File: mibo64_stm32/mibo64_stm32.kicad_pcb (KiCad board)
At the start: 2 copper layers, 73.7 x 20.3 mm, 36 parts, among them J1 Conn_01x02, J2 Conn_01x29, J3 Conn_01x29, J4 USB_B_Micro, J5 Conn_01x04, SW1 Reset, U1 STM32F405RGTx, U2 AMS1117-3.3, Y1 8MHz, Y2 32.768kHz

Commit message: almost fully routed
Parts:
- C12, C13: value 1uF -> 2.2uF
- moved C12 19.5 mm to (133.4, 119.3)
- moved R4 10.1 mm to (137.4, 106.6), turned to 180 degrees
- moved C13 8.16 mm to (151.4, 115.8)
- moved C11 7.67 mm to (163.6, 117.3), turned to 180 degrees
- moved C8 6.37 mm to (167.4, 117.3)
- moved C4 6.34 mm to (147.4, 106.9), turned to 180 degrees
- moved R2 5.76 mm to (155.7, 111.3), turned to 90 degrees
- moved C5 5.39 mm to (152.1, 113.0), turned to 90 degrees
- moved SW1 5.34 mm to (158.8, 112.8), turned to 270 degrees
- moved C3 4.44 mm to (155.7, 114.5), turned to 270 degrees
- moved C7 3.84 mm to (133.2, 115.4), turned to 180 degrees
- moved U2 3.07 mm to (165.4, 111.8)
- moved J1 2.54 mm to (111.8, 111.8), turned to 180 degrees
- moved C10 2.49 mm to (121.9, 108.7), turned to 270 degrees
- moved Y2 2.01 mm to (118.1, 108.0)
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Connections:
- J2 pad 10: /PA5 -> /PB0
- J2 pad 11: /PA6 -> /PB1
- J2 pad 12: /PA7 -> /PB11
- J2 pad 13: /PA8 -> /PB10
- J2 pad 14: /PA9 -> /PB2
- J2 pad 15: /PA10 -> /PB12
- J2 pad 16: /PA11 -> /PB13
- J2 pad 17: /PA12 -> /PB14
- J2 pad 18: /PA15 -> /PB15
- J2 pad 19: /PC0 -> /PC6
- J2 pad 20: /PC1 -> /PC7
- J2 pad 21: /PC2 -> /PC8
- J2 pad 22: /PC3 -> /PC9
- J2 pad 23: /PC4 -> /PA8
- J2 pad 24: /PC5 -> /PA9
- J2 pad 25: /PC6 -> /PA10
- J2 pad 26: /PC7 -> /PA11
- J2 pad 27: /OSC32_IN -> /PA12
- J2 pad 3: /RESET -> /PA3
- J2 pad 4: /VBAT -> /PA4
- J2 pad 5: /PA0 -> /PA5
- J2 pad 6: /PA1 -> /PA6
- J2 pad 7: /PA2 -> /PA7
- J2 pad 8: /PA3 -> /PC4
- J2 pad 9: /PA4 -> /PC5
- J3 pad 10: /PB5 -> /PC3
- J3 pad 11: /PB6 -> /PC2
- J3 pad 12: /PB7 -> /PC1
- J3 pad 13: /PB8 -> /PC0
- J3 pad 14: /PB9 -> /VBAT
- J3 pad 15: /PB10 -> /PB8
- J3 pad 16: /PB11 -> /PB9
- J3 pad 17: /PB12 -> /PB7
- J3 pad 18: /PB13 -> /PB6
- J3 pad 19: /PB14 -> /PB5
- J3 pad 20: /PB15 -> /PB4
- J3 pad 21: /PC8 -> /PB3
- J3 pad 22: /PC9 -> /PD2
- J3 pad 23: /PC10 -> /PC12
- J3 pad 25: /PC12 -> /PC10
- J3 pad 26: /LED1 -> /PA15
- J3 pad 27: /OSC32_OUT -> /LED1
- J3 pad 4: /PD2 -> /OSC32_IN
- J3 pad 5: /PB0 -> /OSC32_OUT
- J3 pad 6: /PB1 -> /RESET
- J3 pad 7: /PB2 -> /PA2
- J3 pad 8: /PB3 -> /PA1
- J3 pad 9: /PB4 -> /PA0
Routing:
- net GND: track 0.00 -> 40.4 mm, vias 0 -> 13
- net /LED1: track 0.00 -> 37.7 mm, vias 0 -> 2
- net +3V3: track 0.00 -> 33.5 mm, vias 0 -> 6
- net /RESET: track 0.00 -> 33.0 mm
- net /PA15: track 0.00 -> 32.8 mm, vias 0 -> 1
- net /PA12: track 0.00 -> 30.6 mm
- net /PA3: track 0.00 -> 29.0 mm
- net /PA11: track 0.00 -> 27.9 mm
- net /PA4: track 0.00 -> 25.9 mm
- net /PA5: track 0.00 -> 23.5 mm
- net /PA10: track 0.00 -> 22.9 mm
- net /PC10: track 0.00 -> 22.2 mm
- net /PA6: track 0.00 -> 21.2 mm
- net /PA9: track 0.00 -> 20.5 mm
- net /PC11: track 0.00 -> 19.9 mm
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- added copper zone on B.Cu, net GND
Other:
- net class Default: clearance 0.2 -> 0.152; trace_width 0.25 -> 0.152; via_dia 0.8 -> 0.6; via_drill 0.4 -> 0.3
- net class power added: clearance 0.152, trace_width 0.4, via_dia 0.8, via_drill 0.5
- rule trace_clearance: 0.2 -> 0.152
- rule trace_min: 0.2 -> 0.152
- board text added: "GND"

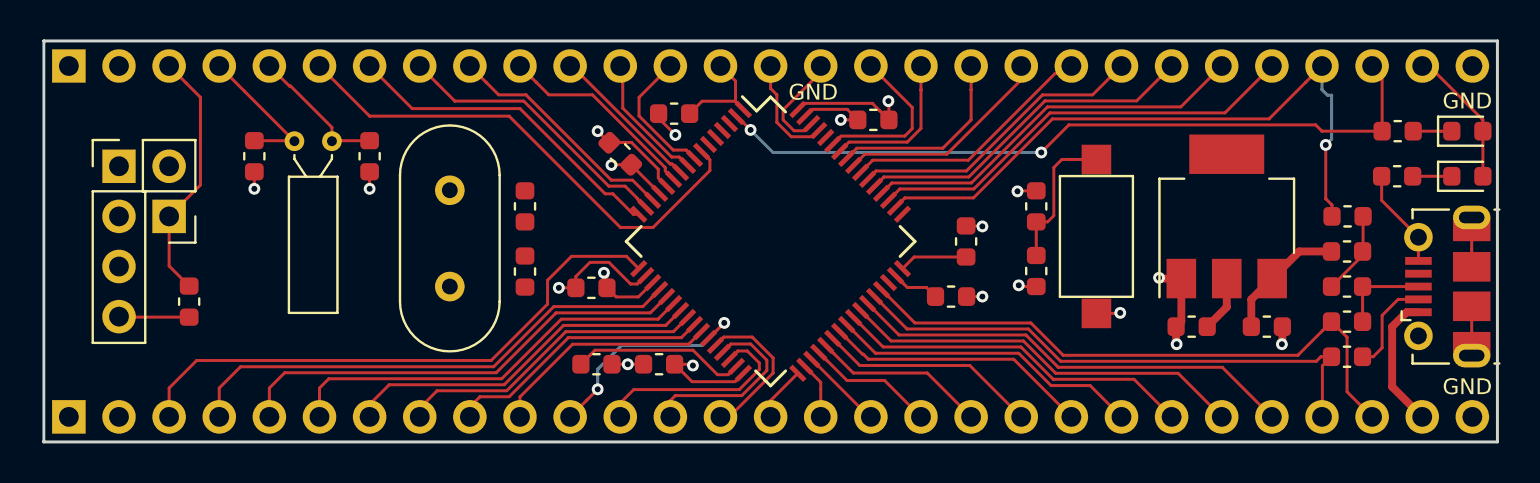
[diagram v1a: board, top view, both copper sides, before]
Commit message: fully routed, labelling still missing
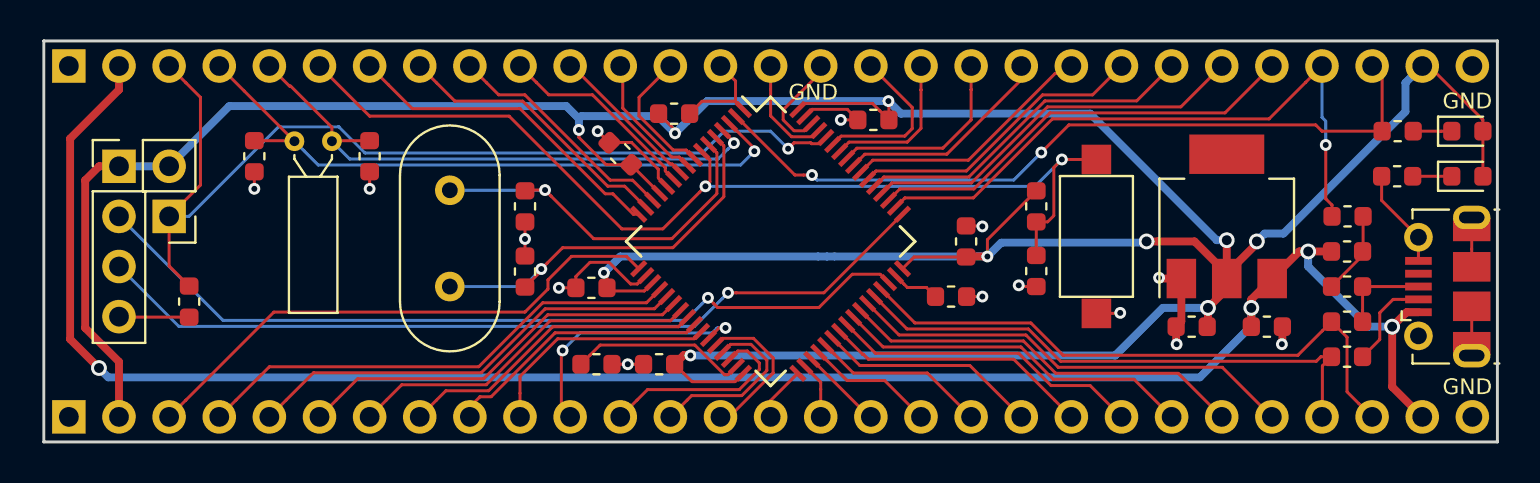
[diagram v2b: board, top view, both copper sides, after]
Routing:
- net +3V3: track 33.5 -> 194.8 mm, vias 6 -> 10
- net /5V: track 13.3 -> 97.1 mm, vias 0 -> 4
- net /SWDCLK: track 0.00 -> 43.3 mm, vias 0 -> 1
- net /SWDIO: track 0.00 -> 42.7 mm, vias 0 -> 1
- net /BOOT0: track 12.9 -> 49.7 mm, vias 0 -> 1
- net /OSC32_IN: track 7.43 -> 33.4 mm, vias 0 -> 1
- net /OSC32_OUT: track 7.08 -> 29.0 mm, vias 0 -> 1
- net /OSC_IN: track 0.00 -> 20.2 mm, vias 0 -> 1
- net /OSC_OUT: track 0.00 -> 19.2 mm, vias 0 -> 1
- net /RESET: track 33.0 -> 52.0 mm, vias 0 -> 2
- net /PB1: track 11.5 -> 13.4 mm
- net GND: track 40.4 -> 42.1 mm, vias 13 -> 14
- net /PA3: track 29.0 -> 27.7 mm
- net /LED1: track 37.7 -> 38.9 mm
- net /PA4: track 25.9 -> 25.0 mm
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
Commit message: MIBO64-STM32 finished.
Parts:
- moved J5 2.54 mm to (111.8, 109.2)
- moved J1 2.54 mm to (114.3, 111.8)
- moved R1 2.17 mm to (114.8, 115.3)
- moved C9 1.02 mm to (117.1, 108.7)
- moved Y2 0.70 mm to (118.8, 108.0)
- moved C10 0.51 mm to (122.4, 108.7)
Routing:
- net GND: track 42.1 -> 39.3 mm, vias 14 -> 15
- net /SWDCLK: track 43.3 -> 41.0 mm
- net /BOOT0: track 49.7 -> 47.9 mm
- net /5V: track 97.1 -> 95.9 mm
- net /SWDIO: track 42.7 -> 41.7 mm
- net /OSC32_OUT: track 29.0 -> 28.4 mm
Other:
- board text added: "3.3"
- board text added: "3.3V"
- board text added: "5V"
- board text added: "A0"
- board text added: "A1"
- board text added: "A10"
- board text added: "A11"
- board text added: "A12"
- board text added: "A15"
- board text added: "A2"
- board text added: "A3"
- board text added: "A4"
- board text added: "A5"
- board text added: "A6"
- board text added: "A7"
- board text added: "A8"
- board text added: "A9"
- board text added: "B0"
- board text added: "B1"
- board text added: "B10"
- board text added: "B11"
- board text added: "B12"
- board text added: "B13"
- board text added: "B14"
- board text added: "B15"
- board text added: "B2"
- board text added: "B3"
- board text added: "B4"
- board text added: "B5"
- board text added: "B6"
- board text added: "B7"
- board text added: "B8"
- board text added: "B9"
- board text added: "C0"
- board text added: "C1"
- board text added: "C10"
- board text added: "C11"
- board text added: "C12"
- board text added: "C13"
- board text added: "C14"
- board text added: "C15"
- board text added: "C2"
- board text added: "C3"
- board text added: "C4"
- board text added: "C5"
- board text added: "C6"
- board text added: "C7"
- board text added: "C8"
- board text added: "C9"
- board text added: "D2"
- board text added: "MIBO64-STM32"
- board text added: "ROM BL."
- board text added: "RST"
- board text added: "SWDCLK"
- board text added: "SWDIO"
- board text added: "VBAT"
- board text added: "boot0"
- board text added: "by nvitya"
